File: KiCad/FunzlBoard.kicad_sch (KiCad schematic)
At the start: 66 parts, among them SW1 SW_MEC_5E, SW2 SW_MEC_5E, SW3 SW_MEC_5E, SW4 SW_MEC_5E, SW5 SW_MEC_5E, U1 ESP32-C3_SUPERMINI_SMD, U2 ADS7828, U3 MCP23017_SO

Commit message: Move a screw
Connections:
- net GND: now also SW1.4 (A), SW2.4 (A), SW3.4 (A), SW4.4 (A), SW5.4 (A)
- net at SW5.1: now also SW5.2, U3.5 (GPB4)
- net at SW1.1: now also SW1.2, U3.1 (GPB0)
- net at SW4.1: now also SW4.2, U3.4 (GPB3)
- net at SW2.2, U3.2 (GPB1): now also SW2.1
- net at SW3.2, U3.3 (GPB2): now also SW3.1
- no-connect marks 13 -> 3
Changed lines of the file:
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@@
 	(generator_version "9.0")
 	(paper "A3")
-	(no_connect
-		(at 292.1 100.33)
-	)
-	(no_connect
-		(at 314.96 100.33)
+	(junction
+		(at 289.56 102.87)
+		(diameter 0)
+		(color 0 0 0 0)
+	)
+	(junction
+		(at 327.66 102.87)
+		(diameter 0)
+		(color 0 0 0 0)
+	)
+	(junction
+		(at 292.1 102.87)
+		(diameter 0)
+		(color 0 0 0 0)
+	)
+	(junction
+		(at 304.8 102.87)
+		(diameter 0)
+		(color 0 0 0 0)
+	)
+	(junction
+		(at 314.96 102.87)
+		(diameter 0)
+		(color 0 0 0 0)
+	)
+	(junction
+		(at 330.2 102.87)
+		(diameter 0)
+		(color 0 0 0 0)
+	)
+	(junction
+		(at 279.4 102.87)
+		(diameter 0)
+		(color 0 0 0 0)
+	)
+	(junction
+		(at 317.5 102.87)
+		(diameter 0)
+		(color 0 0 0 0)
+	)
+	(junction
+		(at 340.36 102.87)
+		(diameter 0)
+		(color 0 0 0 0)
+	)
+	(junction
+		(at 302.26 102.87)
+		(diameter 0)
+		(color 0 0 0 0)
 	)
 	(no_connect
@@
 	)
 	(no_connect
-		(at 340.36 100.33)
-	)
-	(no_connect
-		(at 302.26 100.33)
-	)
-	(no_connect
 		(at 231.14 138.43)
-	)
-	(no_connect
-		(at 330.2 100.33)
 	)
 	(no_connect
 		(at 231.14 140.97)
 	)
-	(no_connect
-		(at 317.5 100.33)
-	)
-	(no_connect
-		(at 279.4 100.33)
-	)
-	(no_connect
-		(at 327.66 100.33)
-	)
-	(no_connect
-		(at 289.56 100.33)
-	)
-	(no_connect
-		(at 304.8 100.33)
-	)
 	(wire
 		(pts
@@
 	(wire
 		(pts
+			(xy 302.26 100.33) (xy 302.26 102.87)
+		)
+		(stroke
+			(width 0)
+			(type default)
+		)
+	)
+	(wire
+		(pts
 			(xy 15.24 140.97) (xy 15.24 30.48)
 		)
@@
 	(wire
 		(pts
+			(xy 292.1 100.33) (xy 292.1 102.87)
+		)
+		(stroke
+			(width 0)
+			(type default)
+		)
+	)
+	(wire
+		(pts
 			(xy 266.7 133.35) (xy 330.2 133.35)
 		)
@@
 	(wire
 		(pts
+			(xy 304.8 100.33) (xy 304.8 102.87)
+		)
+		(stroke
+			(width 0)
+			(type default)
+		)
+	)
+	(wire
+		(pts
 			(xy 185.42 138.43) (xy 172.72 138.43)
 		)
@@
 	(wire
 		(pts
+			(xy 289.56 100.33) (xy 289.56 102.87)
+		)
+		(stroke
+			(width 0)
+			(type default)
+		)
+	)
+	(wire
+		(pts
+			(xy 317.5 100.33) (xy 317.5 102.87)
+		)
+		(stroke
+			(width 0)
+			(type default)
+		)
+	)
+	(wire
+		(pts
 			(xy 185.42 130.81) (xy 176.53 130.81)
 		)
@@
 	(wire
 		(pts
+			(xy 314.96 100.33) (xy 314.96 102.87)
+		)
+		(stroke
+			(width 0)
+			(type default)
+		)
+	)
+	(wire
+		(pts
+			(xy 330.2 100.33) (xy 330.2 102.87)
+		)
+		(stroke
+			(width 0)
+			(type default)
+		)
+	)
+	(wire
+		(pts
+			(xy 327.66 100.33) (xy 327.66 102.87)
+		)
+		(stroke
+			(width 0)
+			(type default)
+		)
+	)
+	(wire
+		(pts
 			(xy 185.42 128.27) (xy 177.8 128.27)
 		)
@@
 	(wire
 		(pts
+			(xy 340.36 100.33) (xy 340.36 102.87)
+		)
+		(stroke
+			(width 0)
+			(type default)
+		)
+	)
+	(wire
+		(pts
 			(xy 142.24 107.95) (xy 142.24 102.87)
 		)
@@
 		)
 		(stroke
+			(width 0)
+			(type default)
+		)
+	)
+	(wire
+		(pts
+			(xy 279.4 100.33) (xy 279.4 102.87)
+		)
+		(stroke

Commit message: Add Trimmer
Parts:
- RV5: footprint (none) -> Lib:TrimmerH
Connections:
- net +3V3: no longer RV1.1, RV2.1, RV3.1, RV4.1, RV5.1, U2.7 (CH6)
- net GND: no longer U2.8 (CH7)
- net REF: now reaches U2.10 (REF)
- net REF: now also RV1.1, RV2.1, RV3.1, RV4.1, RV5.1
- no-connect marks 3 -> 2

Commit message: Add connectors
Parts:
- removed RV4: R_Potentiometer, symbol Device:R_Potentiometer
- added 1WI1: Banana Plug Cable, TerminalBlock_Phoenix:TerminalBlock_Phoenix_MPT-0,5-3-2.54_1x03_P2.54mm_Horizontal, symbol ESP32Board:1WI Screw_Terminal_01x03
- added C1: 470µF, Capacitor_THT:CP_Radial_D6.3mm_P2.50mm, symbol Device:C_Polarized
- added C2, C3: 330µF, Capacitor_THT:CP_Radial_D6.3mm_P2.50mm, symbol Device:C_Polarized
- added J1: Poti, Lib:Connector3, symbol Connector:Conn_01x03_Socket
- added J10: Slider, Lib:Connector2, symbol Connector:Conn_01x02_Socket
- added J11: Toggle, Lib:Connector2, symbol Connector:Conn_01x02_Socket
- added J12: Button Small, Lib:Connector2, symbol Connector:Conn_01x02_Socket
- added J13: Virb.1, Lib:Connector2, symbol Connector:Conn_01x02_Socket
- added J14: Vibr.2, Lib:Connector2, symbol Connector:Conn_01x02_Socket
- added J15: 5V IN, Lib:Connector2, symbol Connector:Conn_01x02_Socket
- added J16: BAT, Lib:Connector2, symbol Connector:Conn_01x02_Socket
- added J17: LED G, Lib:Connector2, symbol Connector:Conn_01x02_Socket
- added J18: LED R, Lib:Connector2, symbol Connector:Conn_01x02_Socket
- added J19: PWR Switch, Lib:Connector2, symbol Connector:Conn_01x02_Socket
- added J2: Banana Plug Socket 1, Connector_PinHeader_2.54mm:PinHeader_1x01_P2.54mm_Horizontal, symbol Connector:Conn_01x01_Pin
- added J20: BAT Monitor, Lib:Connector2, symbol Connector:Conn_01x02_Socket
- added J21: LED Blink, Lib:Connector2, symbol Connector:Conn_01x02_Socket
- added J22: BZ 1, Lib:Connector2, symbol Connector:Conn_01x02_Socket
- added J23: BZ 2, Lib:Connector2, symbol Connector:Conn_01x02_Socket
- added J24: BZ 3, Lib:Connector2, symbol Connector:Conn_01x02_Socket
- added J3: Banana Plug Socket 2, Connector_PinHeader_2.54mm:PinHeader_1x01_P2.54mm_Horizontal, symbol Connector:Conn_01x01_Pin
- added J4: Banana Plug Socket 3, Connector_PinHeader_2.54mm:PinHeader_1x01_P2.54mm_Horizontal, symbol Connector:Conn_01x01_Pin
- added J5: 3-Way, Lib:Connector3, symbol Connector:Conn_01x03_Socket
- added J6: 2-Way 1, Lib:Connector2, symbol Connector:Conn_01x02_Socket
- added J7: 2-Way 2, Lib:Connector2, symbol Connector:Conn_01x02_Socket
- added J8: 2-Way 3, Lib:Connector2, symbol Connector:Conn_01x02_Socket
- added J9: Rocker, Lib:Connector2, symbol Connector:Conn_01x02_Socket
- added Q1, Q2: 2N7002, Package_TO_SOT_SMD:SOT-23, symbol Transistor_FET:2N7002
- added R1: 220R, Resistor_SMD:R_1206_3216Metric, symbol Device:R
- added R2, R3, R4: 33R, Resistor_SMD:R_1206_3216Metric, symbol Device:R
- added TP1: GPIO5, TestPoint:TestPoint_THTPad_D1.5mm_Drill0.7mm, symbol Connector:TestPoint
- added TP2: GPIO6, TestPoint:TestPoint_THTPad_D1.5mm_Drill0.7mm, symbol Connector:TestPoint
- added U4: ~, Lib:Battery_Management, symbol FunzlBoard:Battery_Management
- SW1: value SW_MEC_5E -> Button R
- SW2: value SW_MEC_5E -> Button Y
- SW3: value SW_MEC_5E -> Button G
- SW4: value SW_MEC_5E -> Button B
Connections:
- net +5V: now also C1.1, C2.1, C3.1, J13.2 (Pin_2), J14.2 (Pin_2), J19.2 (Pin_2)
- net GND: now also 1WI1.1 (GND), 1WI1.2 (GND), 1WI1.3 (GND), C1.2, C2.2, C3.2, J1.1 (Pin_1), J10.1 (Pin_1), J11.1 (Pin_1), J12.1 (Pin_1), J21.2 (Pin_2), J22.2 (Pin_2), J23.2 (Pin_2), J24.2 (Pin_2), J5.2 (Pin_2), J6.1 (Pin_1), J7.1 (Pin_1), J8.1 (Pin_1), J9.1 (Pin_1), Q1.2 (S), Q2.2 (S), U4.5 (OUT-); no longer SW5.3 (K), SW5.4 (A)
- net REF: now also J1.3 (Pin_3)
- net at D1.4 (DIN): now also U1.3 (GPIO3); no longer U1.2 (GPIO2)
- net at SW5.1, SW5.2: now also J16.1 (Pin_1), J20.2 (Pin_2), U4.4 (BAT+); no longer U3.5 (GPB4)
- net at U2.4 (CH3): now also J1.2 (Pin_2)
- net at SW1.1, SW1.2: no longer U3.1 (GPB0)
- net at SW4.1, SW4.2: no longer U3.4 (GPB3)
- net at SW2.1, SW2.2: no longer U3.2 (GPB1)
- net at U3.25 (GPA4): now also J12.2 (Pin_2)
- net at U3.26 (GPA5): now also J2.1 (Pin_1)
- net at U3.27 (GPA6): now also J3.1 (Pin_1)
- net at U3.28 (GPA7): now also J4.1 (Pin_1)
- net at SW3.1, SW3.2: no longer U3.3 (GPB2)
- net at U3.6 (GPB5): now also J9.2 (Pin_2)
- net at U3.7 (GPB6): now also J10.2 (Pin_2)
- net at U3.8 (GPB7): now also J11.2 (Pin_2)
- net at U1.0 (GPIO0): now also R2.1
- net at U1.1 (GPIO1): now also R3.1
- net at U1.4 (GPIO4): now also R1.2
- net at U1.5 (GPIO5): now also Q1.1 (G), TP1.1
- net at U1.6 (GPIO6): now also Q2.1 (G), TP2.1
- new net: J17.1 (Pin_1), U4.8 (LED_G)
- new net: J17.2 (Pin_2), J18.2 (Pin_2), U4.7 (LED_GND)
- new net: J22.1 (Pin_1), R2.2
- new net: SW5.3 (K), SW5.4 (A)
- new net: J7.2 (Pin_2), U3.4 (GPB3)
- new net: J15.1 (Pin_1), U4.1 (IN+)
- new net: J15.2 (Pin_2), U4.2 (IN-)
- new net: J16.2 (Pin_2), U4.3 (BAT-)
- new net: J19.1 (Pin_1), U4.6 (OUT+)
- new net: J18.1 (Pin_1), U4.9 (LED_R)
- new net: J23.1 (Pin_1), R3.2
- new net: J13.1 (Pin_1), Q1.3 (D)
- new net: J6.2 (Pin_2), U3.3 (GPB2)
- new net: J21.1 (Pin_1), R1.1
- new net: J5.1 (Pin_1), U3.1 (GPB0)
- new net: J5.3 (Pin_3), U3.2 (GPB1)
- new net: J14.1 (Pin_1), Q2.3 (D)
- new net: J24.1 (Pin_1), R4.2
- new net: J8.2 (Pin_2), U3.5 (GPB4)
- new net: R4.1, U1.2 (GPIO2)
- no-connect marks 2 -> 6
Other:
- moved on the sheet: SW1, SW2, SW3, SW4, SW5

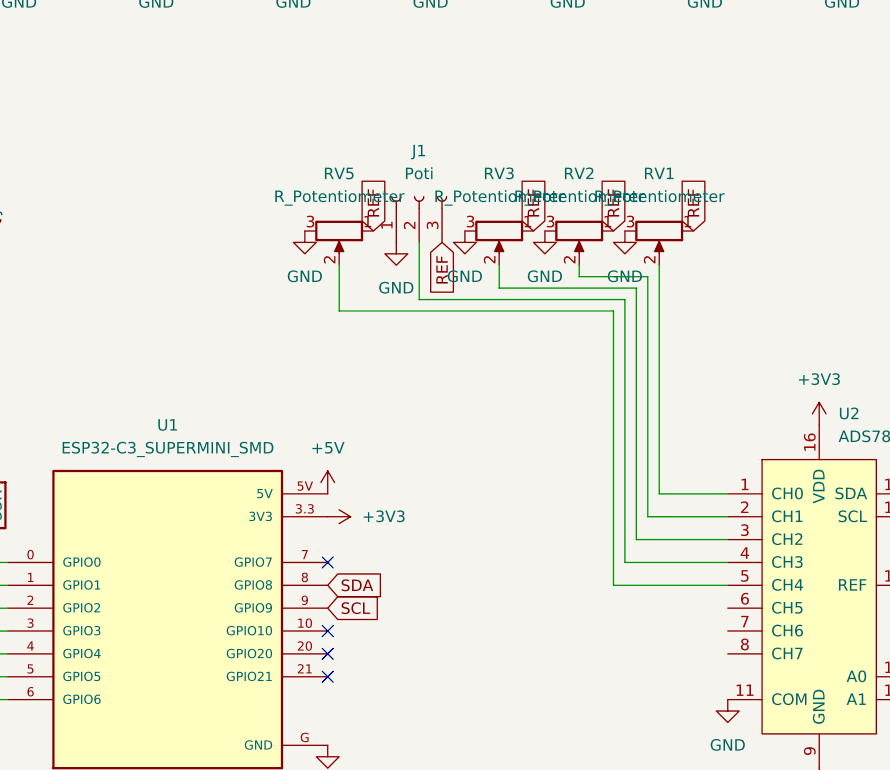
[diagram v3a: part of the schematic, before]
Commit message: Add 2nd trimmer
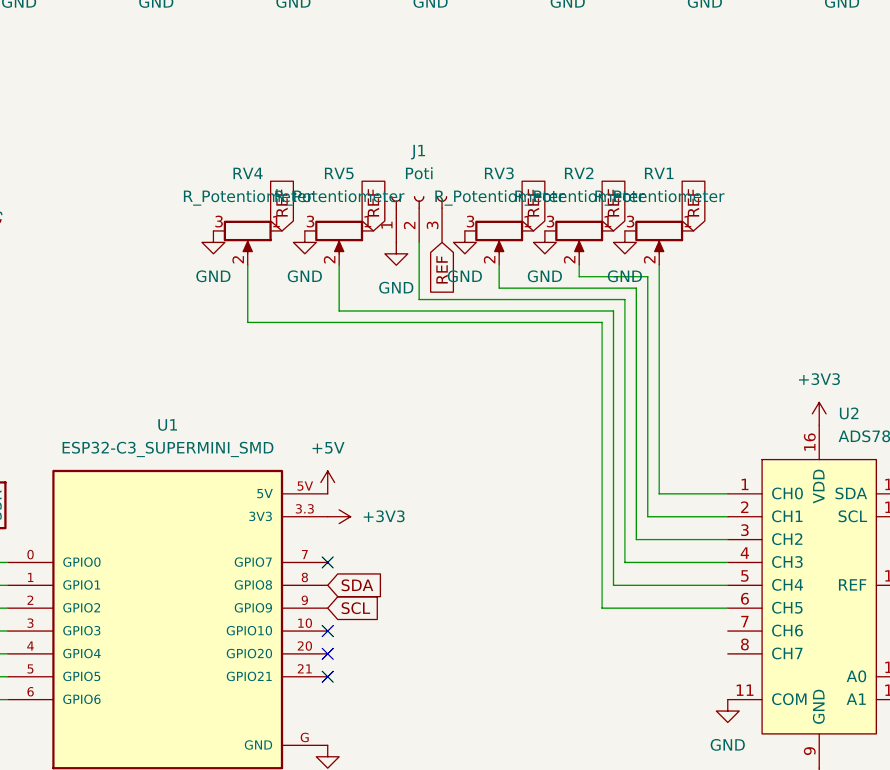
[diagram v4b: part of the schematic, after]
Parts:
- added RV4: R_Potentiometer, Lib:TrimmerH, symbol Device:R_Potentiometer
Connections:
- net GND: now also RV4.3
- net REF: now also RV4.1
- net at U2.6 (CH5): now also RV4.2
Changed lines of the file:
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@@
 	(wire
 		(pts
+			(xy 171.45 140.97) (xy 171.45 109.22)
+		)
+		(stroke
+			(width 0)
+			(type default)
+		)
+	)
+	(wire
+		(pts
 			(xy 78.74 148.59) (xy 78.74 175.26)
 		)
@@
 	(wire
 		(pts
+			(xy 132.08 102.87) (xy 132.08 109.22)
+		)
+		(stroke
+			(width 0)
+			(type default)
+		)
+	)
+	(wire
+		(pts
 			(xy 185.42 135.89) (xy 173.99 135.89)
 		)
@@
 	(wire
 		(pts
+			(xy 185.42 140.97) (xy 171.45 140.97)
+		)
+		(stroke
+			(width 0)
+			(type default)
+		)
+	)
+	(wire
+		(pts
 			(xy 266.7 133.35) (xy 288.29 133.35)
 		)
@@
 	(wire
 		(pts
+			(xy 171.45 109.22) (xy 132.08 109.22)
+		)
+		(stroke
+			(width 0)
+			(type default)
+		)
+	)
+	(wire
+		(pts
 			(xy 160.02 105.41) (xy 160.02 102.87)
 		)
@@
 	(global_label "REF"
 		(shape input)
+		(at 135.89 99.06 90)
+		(fields_autoplaced yes)
+		(effects
+			(font
+				(size 1.27 1.27)
+			)
+			(justify left)
+		)
+		(property "Intersheetrefs" "${INTERSHEET_REFS}"
+			(at 135.89 92.5672 90)
+			(effects
+				(font
+					(size 1.27 1.27)
+				)
+				(justify left)
+				(hide yes)
+			)
+		)
+	)
+	(global_label "REF"
+		(shape input)
 		(at 163.83 99.06 90)
 		(fields_autoplaced yes)
@@
 	)
 	(symbol
+		(lib_id "Device:R_Potentiometer")
+		(at 132.08 99.06 270)
+		(unit 1)
+		(exclude_from_sim no)
+		(in_bom yes)
+		(on_board yes)
+		(dnp no)
+		(fields_autoplaced yes)
+		(property "Reference" "RV4"
+			(at 132.08 92.71 90)
+			(effects
+				(font
+					(size 1.27 1.27)
+				)
+			)
+		)
+		(property "Value" "R_Potentiometer"
+			(at 132.08 95.25 90)
+			(effects
+				(font
+					(size 1.27 1.27)
+				)
+			)
+		)
+		(property "Footprint" "Lib:TrimmerH"
+			(at 132.08 99.06 0)
+			(effects
+				(font
+					(size 1.27 1.27)
+				)
+				(hide yes)
+			)
+		)
+		(property "Datasheet" "~"
+			(at 132.08 99.06 0)
+			(effects
+				(font
+					(size 1.27 1.27)
+				)
+				(hide yes)
+			)
+		)
+		(property "Description" "Potentiometer"
+			(at 132.08 99.06 0)
+			(effects
+				(font
+					(size 1.27 1.27)
+				)
+				(hide yes)
+			)
+		)
+		(pin "2"
+		)
+		(pin "1"
+		)
+		(pin "3"
+		)
+		(instances
+			(project "FunzlBoard"
+				(path "/969bb173-34d7-4b46-8a59-72ed8ea1ad7c"
+					(reference "RV4")
+					(unit 1)
+				)
+			)
+		)
+	)
+	(symbol
 		(lib_id "Analog_ADC:ADS7828")
 		(at 195.58 138.43 0)
@@
 					(unit 1)
 				)
+			)
+		)
+	)
+	(symbol
+		(lib_id "power:GND")
+		(at 128.27 99.06 0)
+		(unit 1)
+		(exclude_from_sim no)
+		(in_bom yes)
+		(on_board yes)
+		(dnp no)
+		(fields_autoplaced yes)
+		(property "Reference" "#PWR0135"
+			(at 128.27 105.41 0)
+			(effects
+				(font
+					(size 1.27 1.27)
+				)
+				(hide yes)
+			)
+		)
+		(property "Value" "GND"
+			(at 128.27 104.14 0)
+			(effects
+				(font
+					(size 1.27 1.27)
+				)
+			)
+		)
+		(property "Footprint" ""
+			(at 128.27 99.06 0)
+			(effects
+				(font
+					(size 1.27 1.27)
+				)
+				(hide yes)
+			)
+		)
+		(property "Datasheet" ""
+			(at 128.27 99.06 0)
+			(effects
+				(font
+					(size 1.27 1.27)
+				)
+				(hide yes)
+			)
+		)
+		(property "Description" "Power symbol creates a global label with name \"GND\" , ground"
+			(at 128.27 99.06 0)
+			(effects
+				(font
+					(size 1.27 1.27)
+				)
+				(hide yes)
+			)
+		)
+		(pin "1"
+		)
+		(instances
+			(project "FunzlBoard"
+				(path "/969bb173-34d7-4b46-8a59-72ed8ea1ad7c"
+					(reference "#PWR0135")
+					(unit 1)
+				)

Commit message: Place capas
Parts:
- added C10, C11, C12, C13, C14, C15, C16, C17, C18, C19, C20, C21, C22, C23, C24, C25, C26, C27, C28, C29, C30, C31, C32, C33, C34, C35, C36, C37, C38, C39, C4, C40, C41, C42, C43, C44, C45, C46, C47, C48, C49, C5, C8, C9: 100nF, Capacitor_SMD:C_1206_3216Metric, symbol Device:C
- added C6, C7: 330µF, Capacitor_THT:CP_Radial_D6.3mm_P2.50mm, symbol Device:C_Polarized
- added R5, R6: 4K7, Resistor_SMD:R_1206_3216Metric, symbol Device:R
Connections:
- net +3V3: now also C4.1, C5.1, C7.1, R5.1, R6.1
- net +5V: now also C10.1, C11.1, C12.1, C13.1, C14.1, C15.1, C16.1, C17.1, C18.1, C19.1, C20.1, C21.1, C22.1, C23.1, C24.1, C25.1, C26.1, C27.1, C28.1, C29.1, C30.1, C31.1, C32.1, C33.1, C34.1, C35.1, C36.1, C37.1, C38.1, C39.1, C40.1, C41.1, C42.1, C43.1, C44.1, C45.1, C46.1, C47.1, C48.1, C49.1, C6.1, C8.1, C9.1
- net GND: now also C10.2, C11.2, C12.2, C13.2, C14.2, C15.2, C16.2, C17.2, C18.2, C19.2, C20.2, C21.2, C22.2, C23.2, C24.2, C25.2, C26.2, C27.2, C28.2, C29.2, C30.2, C31.2, C32.2, C33.2, C34.2, C35.2, C36.2, C37.2, C38.2, C39.2, C4.2, C40.2, C41.2, C42.2, C43.2, C44.2, C45.2, C46.2, C47.2, C48.2, C49.2, C5.2, C6.2, C7.2, C8.2, C9.2
- net SCL: now also R5.2
- net SDA: now also R6.2
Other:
- moved on the sheet: C1, C2, C3

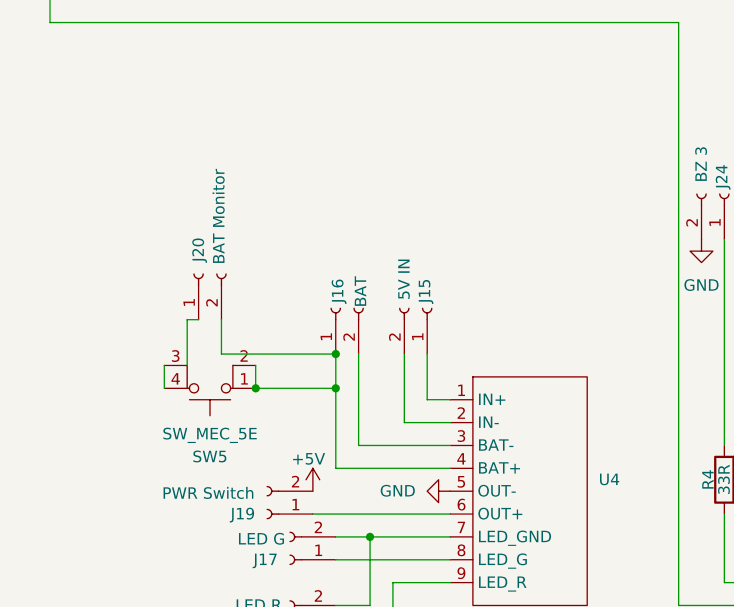
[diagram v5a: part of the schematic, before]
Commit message: Add fuse
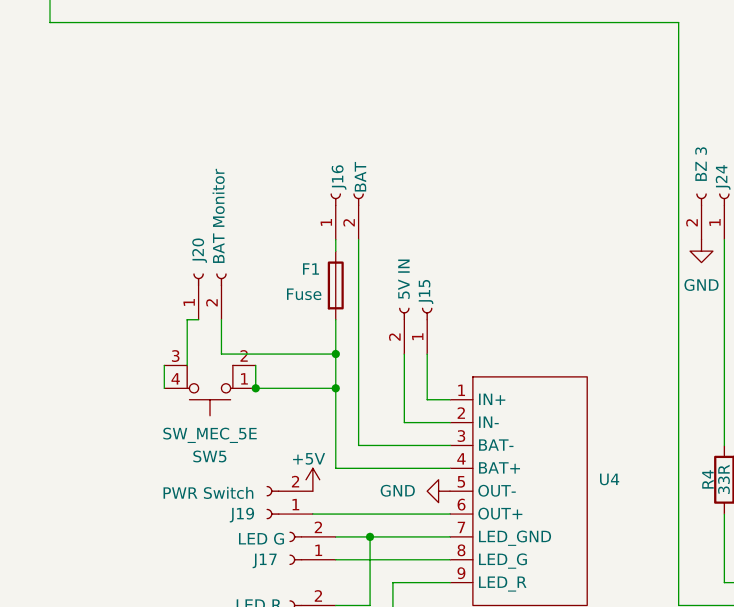
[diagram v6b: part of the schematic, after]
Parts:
- added F1: Fuse, Fuse:Fuseholder_Clip-5x20mm_Littelfuse_111_Inline_P20.00x5.00mm_D1.05mm_Horizontal, symbol Device:Fuse
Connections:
- net at J20.2 (Pin_2), SW5.1, SW5.2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: now also F1.2; no longer J16.1 (Pin_1)
- new net: F1.1, J16.1 (Pin_1)
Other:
- moved on the sheet: J16
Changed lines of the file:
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@@
 	(wire
 		(pts
-			(xy 49.53 125.73) (xy 49.53 115.57)
+			(xy 49.53 125.73) (xy 49.53 102.87)
 		)
 		(stroke
@@
 	(wire
 		(pts
+			(xy 46.99 111.76) (xy 46.99 115.57)
+		)
+		(stroke
+			(width 0)
+			(type default)
+		)
+	)
+	(wire
+		(pts
 			(xy 298.45 138.43) (xy 298.45 118.11)
 		)
@@
 	(wire
 		(pts
+			(xy 46.99 102.87) (xy 46.99 104.14)
+		)
+		(stroke
+			(width 0)
+			(type default)
+		)
+	)
+	(wire
+		(pts
 			(xy 104.14 133.35) (xy 104.14 135.89)
 		)
@@
 	(symbol
 		(lib_id "Connector:Conn_01x02_Socket")
-		(at 46.99 110.49 90)
+		(at 46.99 97.79 90)
 		(unit 1)
 		(exclude_from_sim no)
@@
 		(dnp no)
 		(property "Reference" "J16"
-			(at 47.244 107.188 0)
+			(at 47.244 94.488 0)
 			(effects
 				(font
@@
 		)
 		(property "Value" "BAT"
-			(at 49.784 106.934 0)
+			(at 49.784 94.234 0)
 			(effects
 				(font
@@
 		)
 		(property "Footprint" "Lib:Connector2"
-			(at 46.99 110.49 0)
+			(at 46.99 97.79 0)
 			(effects
 				(font
@@
 		)
 		(property "Datasheet" "~"
-			(at 46.99 110.49 0)
+			(at 46.99 97.79 0)
 			(effects
 				(font
@@
 		)
 		(property "Description" "Generic connector, single row, 01x02, script generated"
-			(at 46.99 110.49 0)
+			(at 46.99 97.79 0)
 			(effects
 				(font
@@
 					(unit 1)
 				)
+			)
+		)
+	)
+	(symbol
+		(lib_id "Device:Fuse")
+		(at 46.99 107.95 0)
+		(unit 1)
+		(exclude_from_sim no)
+		(in_bom yes)
+		(on_board yes)
+		(dnp no)
+		(property "Reference" "F1"
+			(at 43.18 106.172 0)
+			(effects
+				(font
+					(size 1.27 1.27)
+				)
+				(justify left)
+			)
+		)
+		(property "Value" "Fuse"
+			(at 41.402 108.966 0)
+			(effects
+				(font
+					(size 1.27 1.27)
+				)
+				(justify left)
+			)
+		)
+		(property "Footprint" "Fuse:Fuseholder_Clip-5x20mm_Littelfuse_111_Inline_P20.00x5.00mm_D1.05mm_Horizontal"
+			(at 45.212 107.95 90)
+			(effects
+				(font
+					(size 1.27 1.27)
+				)
+				(hide yes)
+			)
+		)
+		(property "Datasheet" "~"
+			(at 46.99 107.95 0)
+			(effects
+				(font
+					(size 1.27 1.27)
+				)
+				(hide yes)
+			)
+		)
+		(property "Description" "Fuse"
+			(at 46.99 107.95 0)
+			(effects
+				(font
+					(size 1.27 1.27)
+				)
+				(hide yes)
+			)
+		)
+		(pin "2"
+		)
+		(pin "1"
+		)
+		(instances
+			(project ""
+				(path "/969bb173-34d7-4b46-8a59-72ed8ea1ad7c"
+					(reference "F1")
+					(unit 1)
+				)
